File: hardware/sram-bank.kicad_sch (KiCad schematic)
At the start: 4 parts, among them U1 74AHC1G00GV,125

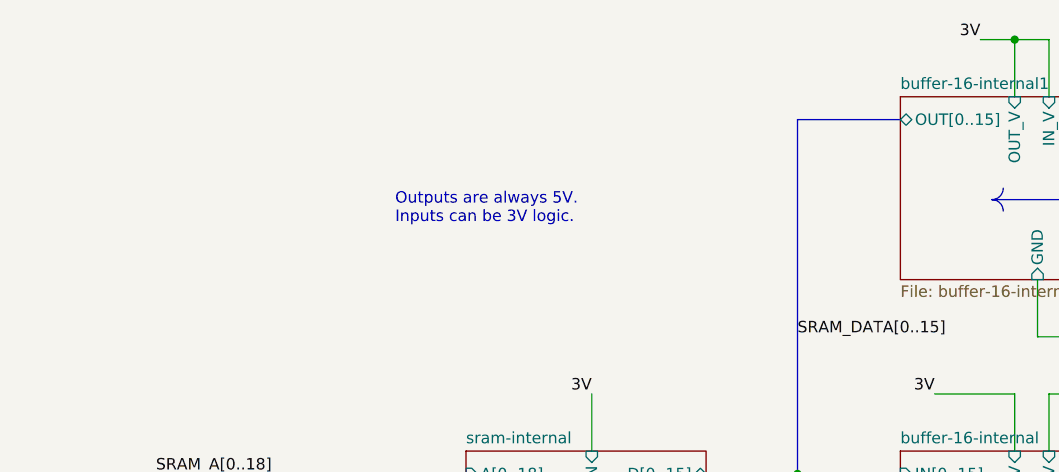
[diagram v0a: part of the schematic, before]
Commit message: Update notes on SRAM schematic
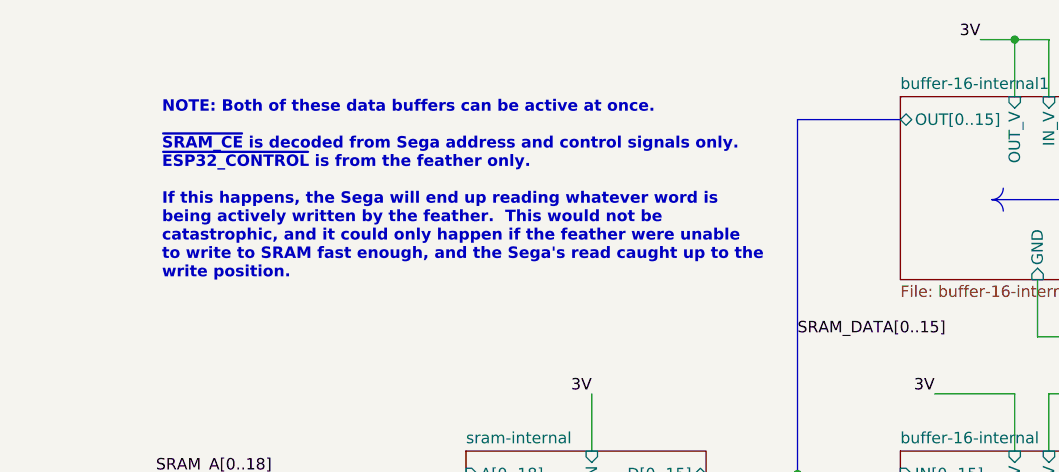
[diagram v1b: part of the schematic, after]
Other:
- note added: "NOTE: Both of these data buffers can be active at once. ~{SRAM_CE} is decoded from Sega address and control signals only. ~{ESP32_CONTROL} is from the feather only. If this happens, the Sega will end up reading whatever word is being actively written by the feather. This would not be catastrophic, and it could only happen if the feather were unable to write to SRAM fast enough, and the Sega's rea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"
- note removed: "Outputs are always 5V. Inputs can be 3V logic."
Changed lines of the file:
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@@
-		)
-	)
-	(text "Outputs are always 5V.\nInputs can be 3V logic."
-		(exclude_from_sim no)
-		(at 77.216 36.576 0)
-		(effects
-			(font
-				(size 1.27 1.27)
-			)
-			(justify left)
 		)
 	)
@@
 		)
 	)
+	(text "NOTE: Both of these data buffers can be active at once.\n\n~{SRAM_CE} is decoded from Sega address and control signals only.\n~{ESP32_CONTROL} is from the feather only.\n\nIf this happens, the Sega will end up reading whatever word is\nbeing actively written by the feather.  This would not be\ncatastrophic, and it could only happen if the feather were unable\nto write to SRAM fast enough, and the Sega's read caught up to the\nwrite position."
+		(exclude_from_sim no)
+		(at 51.308 34.544 0)
+		(effects
+			(font
+				(size 1.27 1.27)
+				(thickness 0.254)
+				(bold yes)
+			)
+			(justify left)
+		)
+	)

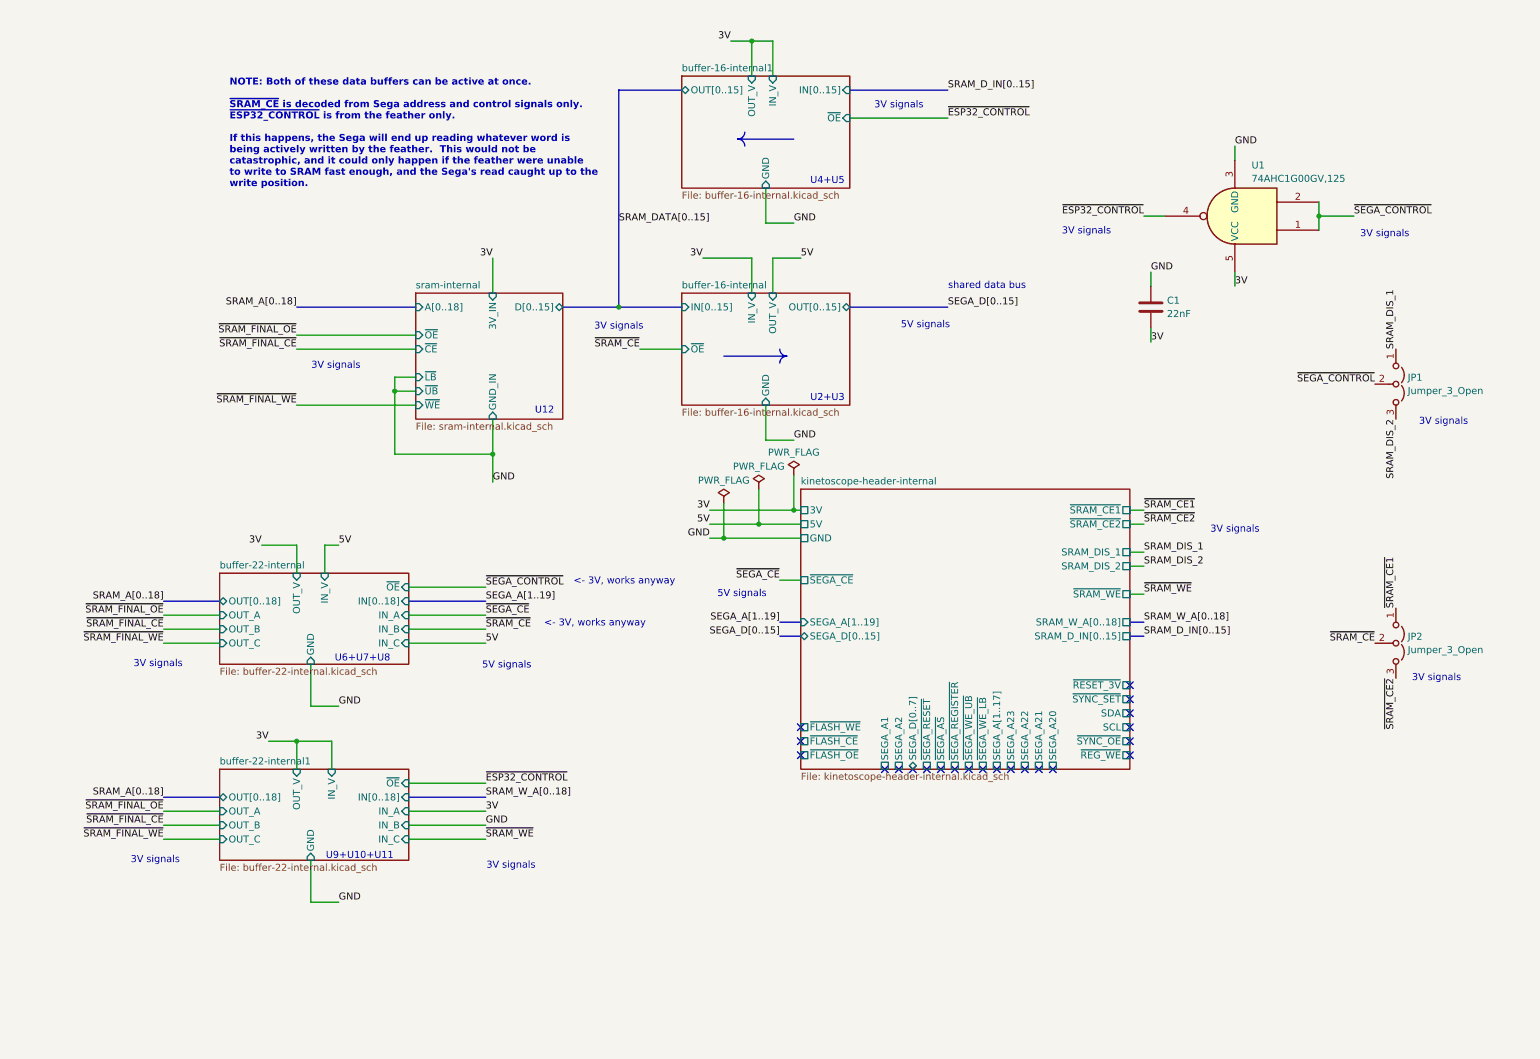
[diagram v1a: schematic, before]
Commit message: Massively reorganize board designs
Now planning to have most assembly done by JLCPCB, so trace sizes,
part selections, etc. are set accordingly.

New boards are:
 - cartridge interface & flash
 - microcontroller & registers
 - sram x2
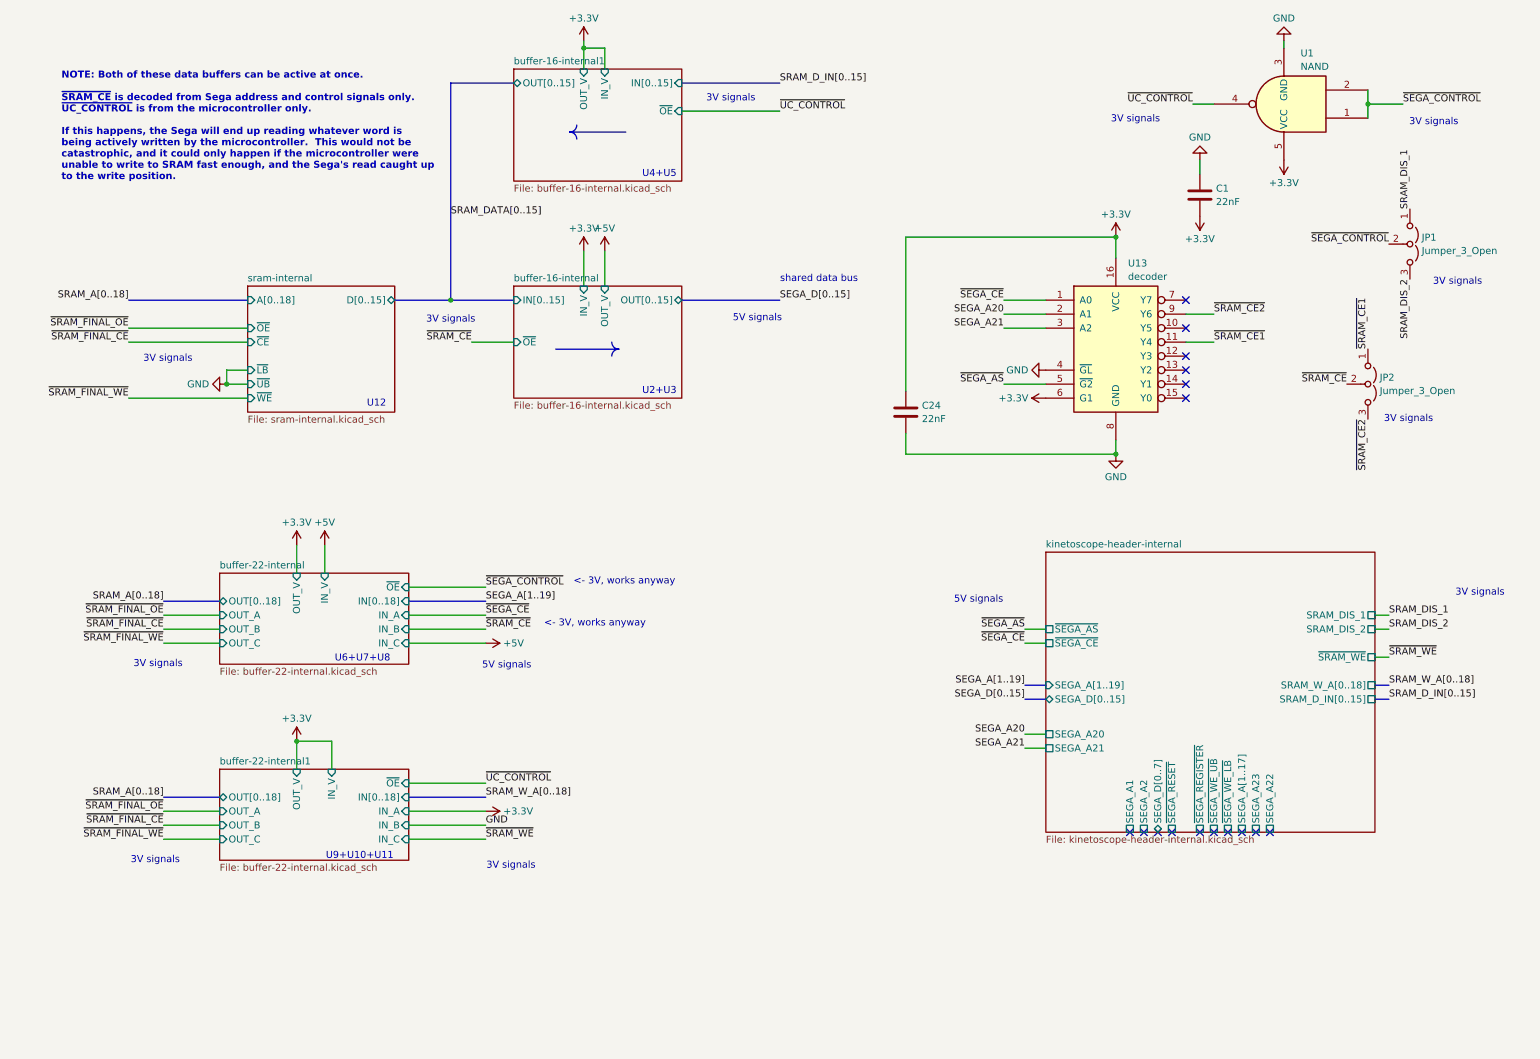
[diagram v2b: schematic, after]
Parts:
- added C24: 22nF, Capacitor_SMD:C_0603_1608Metric, symbol Device:C
- added U13: decoder, Package_SO:SO-16_3.9x9.9mm_P1.27mm, symbol 74xx:74LS137
- C1: footprint Capacitor_SMD:C_1206_3216Metric -> Capacitor_SMD:C_0603_1608Metric; JLCPCB Part Number (none) -> CL10B223KB8NNNC; Mouser Part Number (none) -> 80-C0603C223K4R; Part Number (none) -> C0603C223K4RACTU
- U1: value 74AHC1G00GV,125 -> NAND; JLCPCB Part Number (none) -> C12483; Mouser Part Number (none) -> 771-AHC1G00GV125; Part Number (none) -> 74AHC1G00GV,125
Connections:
- net GND: now also C24.2, U13.4 (~{GL}), U13.8 (GND)
- net ~{SEGA_CE}: now also U13.1 (A0)
- net ~{SRAM_CE1}: now also U13.11 (Y4)
- net ~{SRAM_CE2}: now also U13.9 (Y6)
- net 3V renamed +3.3V
- net +3.3V: now also C24.1, U13.16 (VCC), U13.6 (G1)
- net ~{ESP32_CONTROL} renamed ~{UC_CONTROL}
- new net SEGA_A20: U13.2 (A1)
- new net SEGA_A21: U13.3 (A2)
- new net ~{SEGA_AS}: U13.5 (~{G2})
- no-connect marks 22 -> 16
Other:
- sheet buffer-16-internal ports: added none; removed GND
- sheet buffer-16-internal1 ports: added none; removed GND
- sheet buffer-22-internal ports: added none; removed GND
- sheet buffer-22-internal1 ports: added none; removed GND
- sheet kinetoscope-header-internal ports: added none; removed 3V, 5V, GND, SCL, SDA, ~{FLASH_CE}, ~{FLASH_OE}, ~{FLASH_WE}, ~{REG_WE}, ~{RESET_3V}, ~{SRAM_CE1}, ~{SRAM_CE2}, ~{SYNC_OE}, ~{SYNC_SET}
- sheet sram-internal ports: added none; removed 3V_IN, GND_IN
- note added: "NOTE: Both of these data buffers can be active at once. ~{SRAM_CE} is decoded from Sega address and control signals only. ~{UC_CONTROL} is from the microcontroller only. If this happens, the Sega will end up reading whatever word is being actively written by the microcontroller. This would not be catastrophic, and it could only happen if the microcontroller were unable to write to SRAM fast enoug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"
- note removed: "NOTE: Both of these data buffers can be active at once. ~{SRAM_CE} is decoded from Sega address and control signals only. ~{ESP32_CONTROL} is from the feather only. If this happens, the Sega will end up reading whatever word is being actively written by the feather. This would not be catastrophic, and it could only happen if the feather were unable to write to SRAM fast enough, and the Sega's rea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"
- moved on the sheet: C1, JP1, JP2, U1

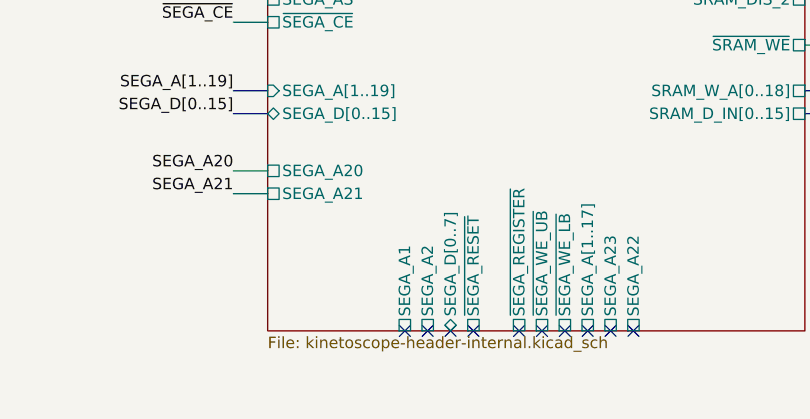
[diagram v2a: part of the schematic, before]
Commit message: Fix out-of-date interboard interface in SRAM schematic
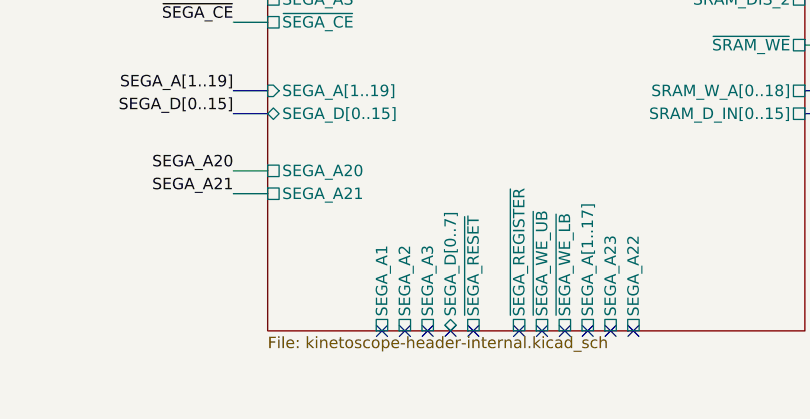
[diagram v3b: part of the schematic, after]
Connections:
- no-connect marks 16 -> 17
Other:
- sheet kinetoscope-header-internal ports: added SEGA_A3; removed none
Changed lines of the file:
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@@
 	)
 	(no_connect
+		(at 212.09 161.29)
+	)
+	(no_connect
 		(at 214.63 161.29)
 	)
@@
 		)
 		(pin "SEGA_A2" passive
-			(at 217.17 161.29 270)
+			(at 214.63 161.29 270)
 			(effects
 				(font
@@
 		)
 		(pin "SEGA_A1" passive
-			(at 214.63 161.29 270)
+			(at 212.09 161.29 270)
+			(effects
+				(font
+					(size 1.27 1.27)
+				)
+				(justify left)
+			)
+		)
+		(pin "SEGA_A3" passive
+			(at 217.17 161.29 270)
 			(effects
 				(font

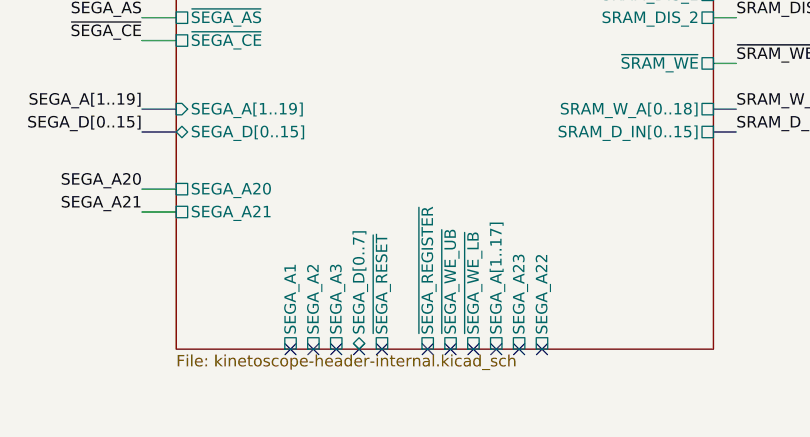
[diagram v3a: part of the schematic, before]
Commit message: Update interboard header in microcontroller and SRAM boards
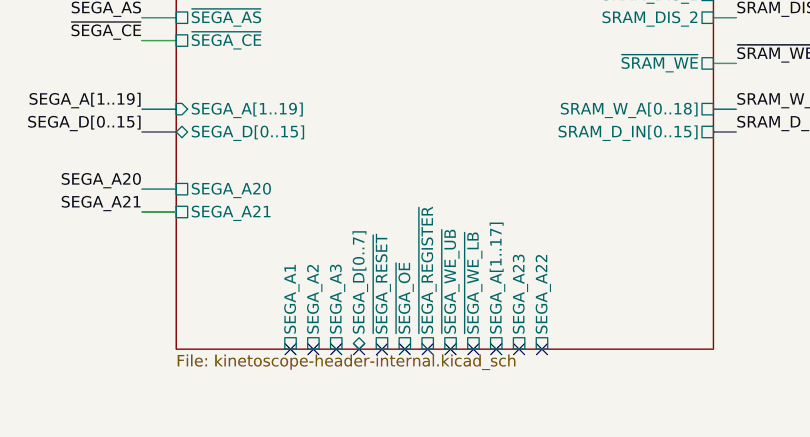
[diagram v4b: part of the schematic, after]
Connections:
- no-connect marks 17 -> 18
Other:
- sheet kinetoscope-header-internal ports: added ~{SEGA_OE}; removed none
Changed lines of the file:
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@@
 	)
 	(no_connect
+		(at 224.79 161.29)
+	)
+	(no_connect
 		(at 232.41 161.29)
 	)
@@
 			(effects
 				(font
+					(size 1.27 1.27)
+				)
+				(justify left)
+			)
+		)
+		(pin "~{SEGA_OE}" passive
+			(at 224.79 161.29 270)
+			(effects
+				(font
